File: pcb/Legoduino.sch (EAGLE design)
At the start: 91 parts, among them CON11 ISP-AVR, CON2 PIN(1+16)X3_DS, IC1 NCP3170ADR2G, IC2 RN-42, IC3 MIC5205-5.0YM5, IC4 ATMEGA2560-16AU, IC5 UG-2864HSWEG01_SPI, IC6 MIC5205-3.6YM5, IC7 MIC5205-3.3YM5, IC8 BD6221F-E2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

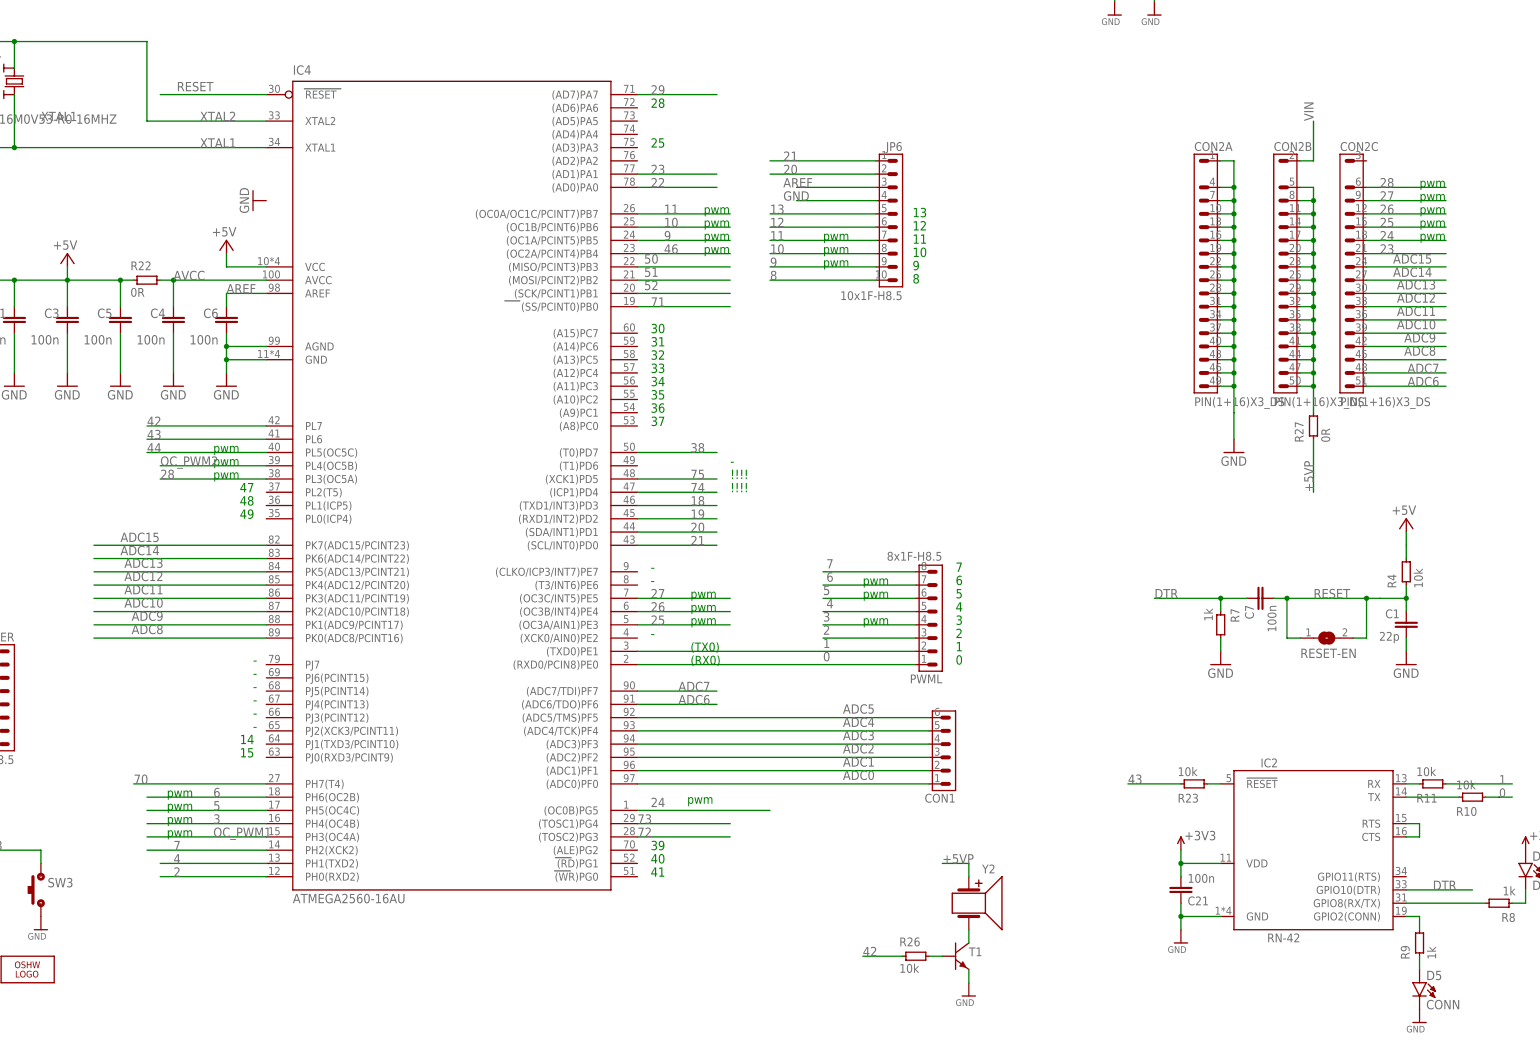
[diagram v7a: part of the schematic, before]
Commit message: #20: Optimized pin assignment and component placement
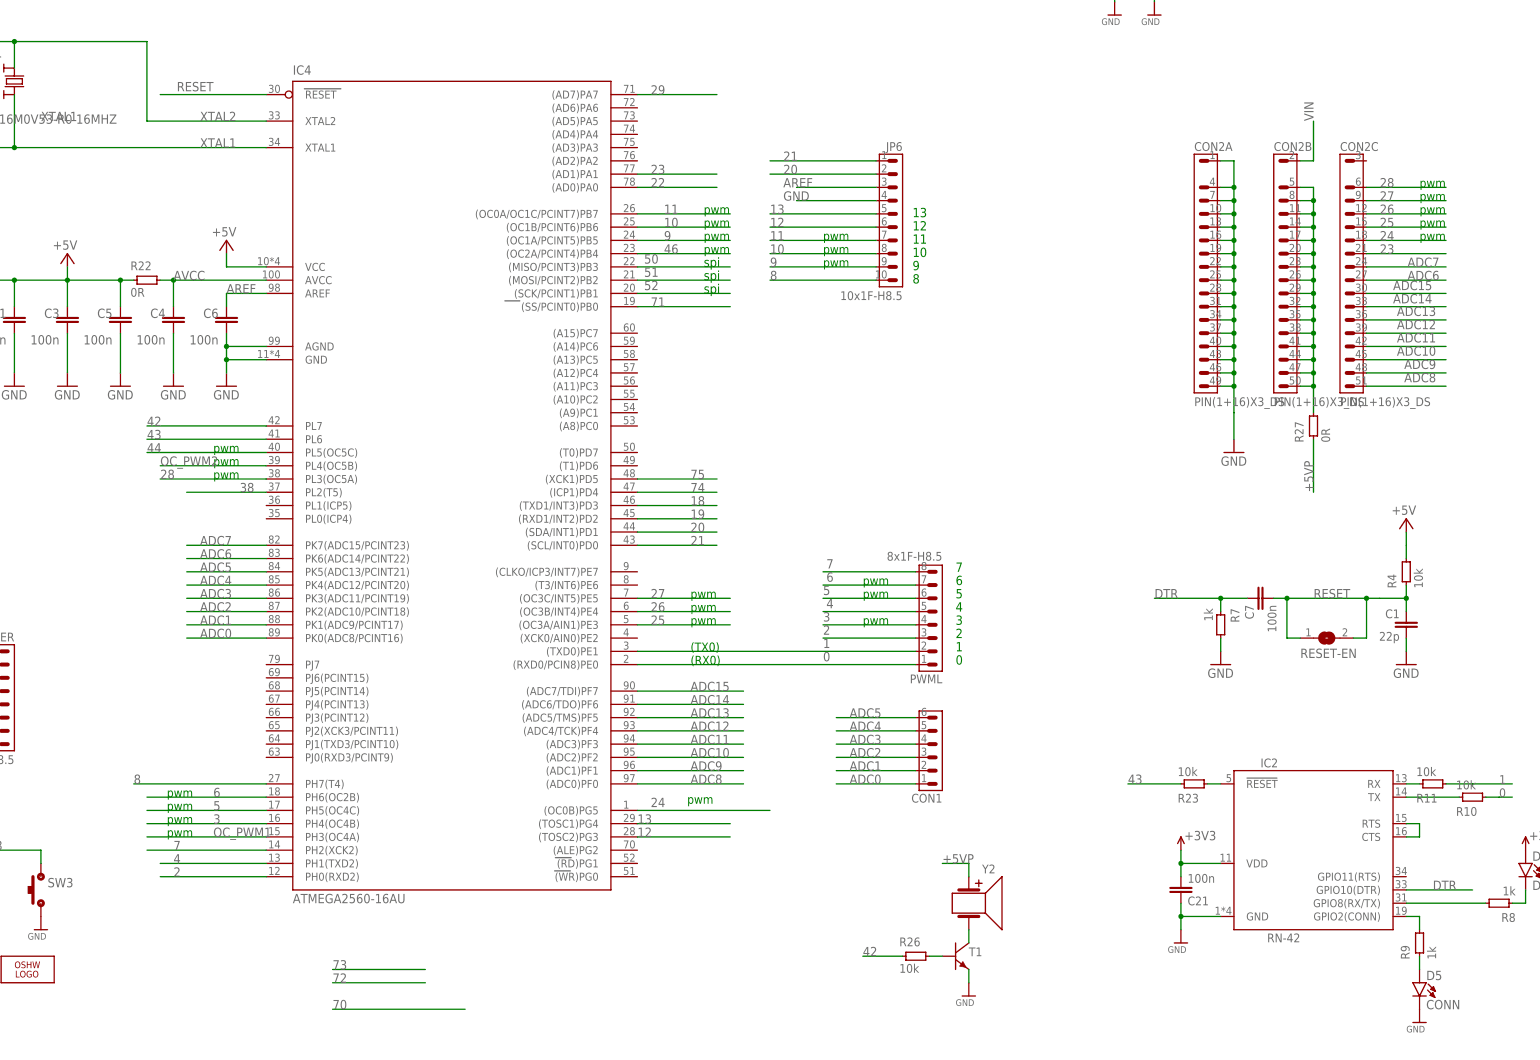
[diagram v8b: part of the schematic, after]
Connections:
- net 12: now also IC4.(TOSC2)PG3
- net 13: now also IC4.(TOSC1)PG4
- net 38: now also IC4.PL2(T5); no longer IC4.(T0)PD7
- net 70: no longer IC4.PH7(T4)
- net 72: no longer IC4.(TOSC2)PG3
- net 73: no longer IC4.(TOSC1)PG4
- net 8: now also IC4.PH7(T4)
- net ADC0: now also IC4.PK0(ADC8/PCINT16); no longer IC4.(ADC0)PF0
- net ADC1: now also IC4.PK1(ADC9/PCINT17); no longer IC4.(ADC1)PF1
- net ADC10: now also CON2C.15, IC4.(ADC2)PF2; no longer CON2C.13, IC4.PK2(ADC10/PCINT18)
- net ADC11: now also CON2C.14, IC4.(ADC3)PF3; no longer CON2C.12, IC4.PK3(ADC11/PCINT19)
- net ADC12: now also CON2C.13, IC4.(ADC4/TCK)PF4; no longer CON2C.11, IC4.PK4(ADC12/PCINT20)
- net ADC13: now also CON2C.12, IC4.(ADC5/TMS)PF5; no longer CON2C.10, IC4.PK5(ADC13/PCINT21)
- net ADC14: now also CON2C.11, IC4.(ADC6/TDO)PF6; no longer CON2C.9, IC4.PK6(ADC14/PCINT22)
- net ADC15: now also CON2C.10, IC4.(ADC7/TDI)PF7; no longer CON2C.8, IC4.PK7(ADC15/PCINT23)
- net ADC2: now also IC4.PK2(ADC10/PCINT18); no longer IC4.(ADC2)PF2
- net ADC3: now also IC4.PK3(ADC11/PCINT19); no longer IC4.(ADC3)PF3
- net ADC4: now also IC4.PK4(ADC12/PCINT20); no longer IC4.(ADC4/TCK)PF4
- net ADC5: now also IC4.PK5(ADC13/PCINT21); no longer IC4.(ADC5/TMS)PF5
- net ADC6: now also CON2C.9, IC4.PK6(ADC14/PCINT22); no longer CON2C.17, IC4.(ADC6/TDO)PF6
- net ADC7: now also CON2C.8, IC4.PK7(ADC15/PCINT23); no longer CON2C.16, IC4.(ADC7/TDI)PF7
- net ADC8: now also CON2C.17, IC4.(ADC0)PF0; no longer CON2C.15, IC4.PK0(ADC8/PCINT16)
- net ADC9: now also CON2C.16, IC4.(ADC1)PF1; no longer CON2C.14, IC4.PK1(ADC9/PCINT17)
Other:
- note added: "spi"
- note removed: "!!!!"
- note removed: "-"
- note removed: "14"
- note removed: "15"
- note removed: "25"
- note removed: "28"
- note removed: "30"
- note removed: "31"
- note removed: "32"
- note removed: "33"
- note removed: "34"
- note removed: "35"
- note removed: "36"
- note removed: "37"
- note removed: "39"
- note removed: "40"
- note removed: "41"
- note removed: "47"
- note removed: "48"
- note removed: "49"
- moved on the sheet: CON1
